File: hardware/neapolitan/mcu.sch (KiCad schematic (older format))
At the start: 63 parts, among them J1 USB-MICRO-B, J11 BARREL_JACK, P1 !IO_INT, P2 !IO_RESET, P20 GPIO, P22 I2S, P28 SD, P5 LEDS, P80 SHIELD, Q5 MOSFET_P, Q6 MOSFET_P, Q7 MOSFET_P, U15 TCA6424A, U16 TCR2EF, U18 74LVC1G14, X2 FOX924B, X3 KT2520, X4 OH4

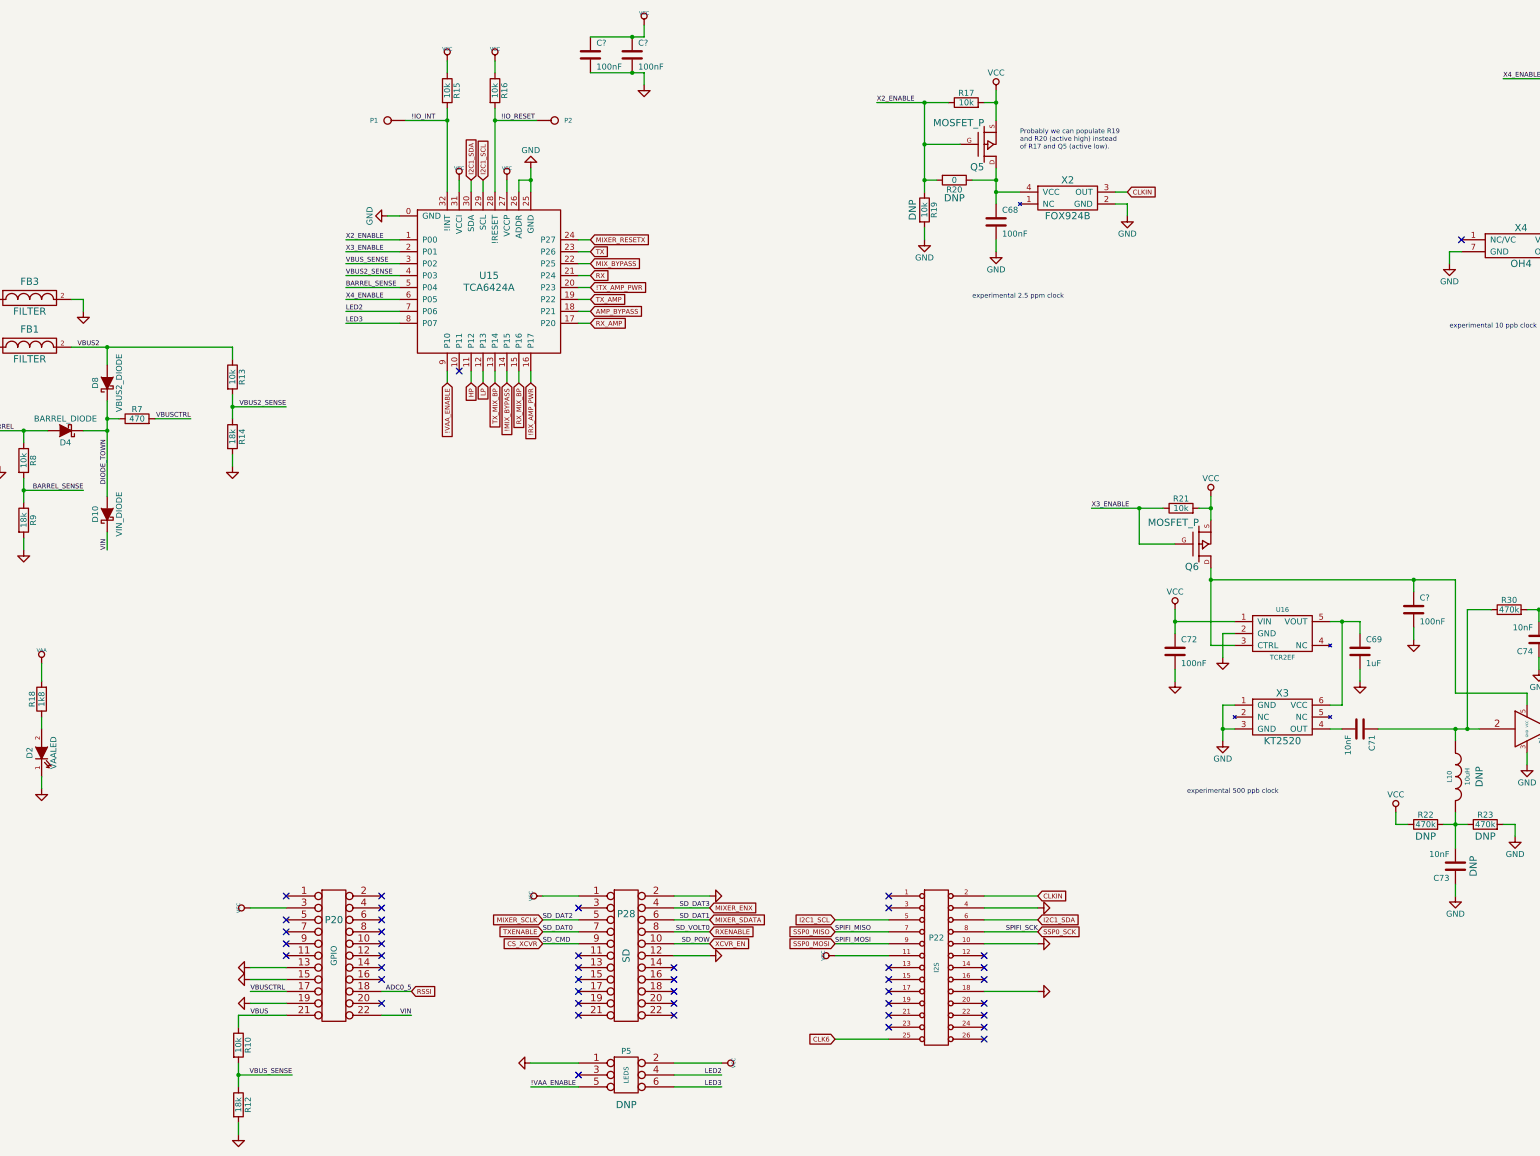
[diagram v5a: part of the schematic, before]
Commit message: Neapolitan: added decoupling caps near pin headers
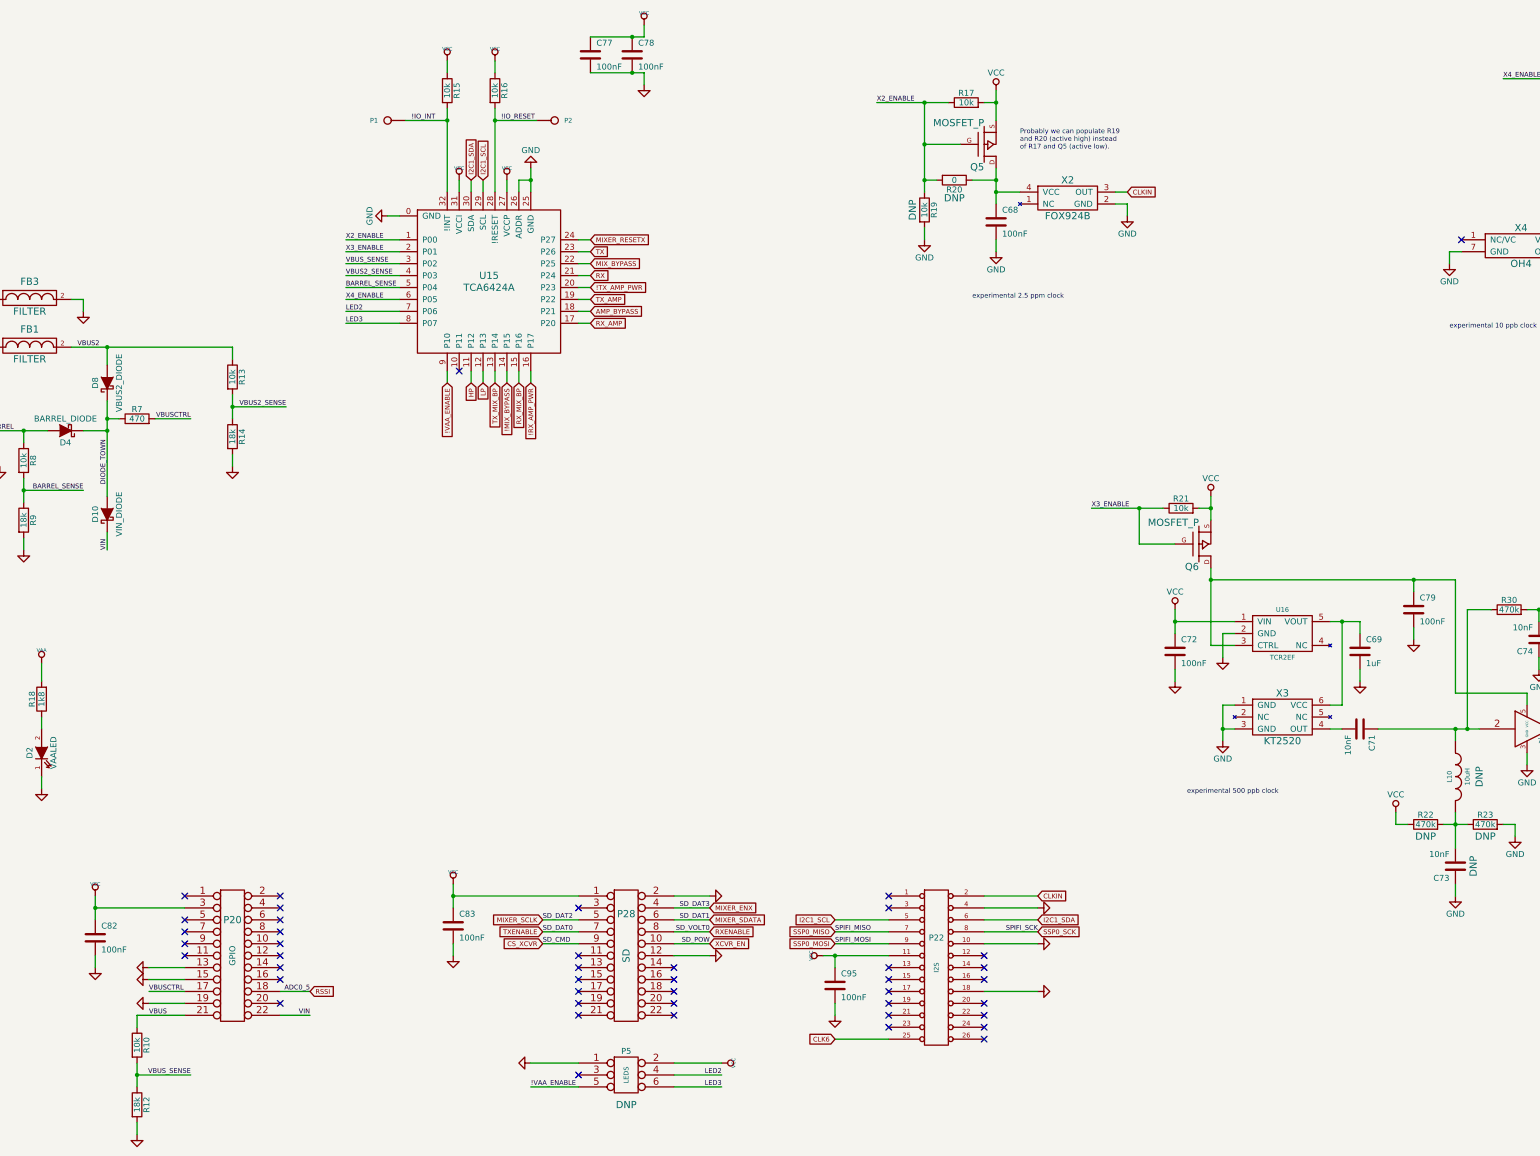
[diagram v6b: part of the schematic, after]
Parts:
- added C82, C83, C95: 100nF, hackrf:GSG-0402, symbol C
- gave numbers to parts that had none: 3
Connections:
- net GND: now also C82.2, C83.2, C95.2
- net VCC: now also C82.1, C83.1, C95.1
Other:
- moved on the sheet: P20, R10, R12
